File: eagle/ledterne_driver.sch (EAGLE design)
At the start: 1 part, among them IC1 MEGA8-AI

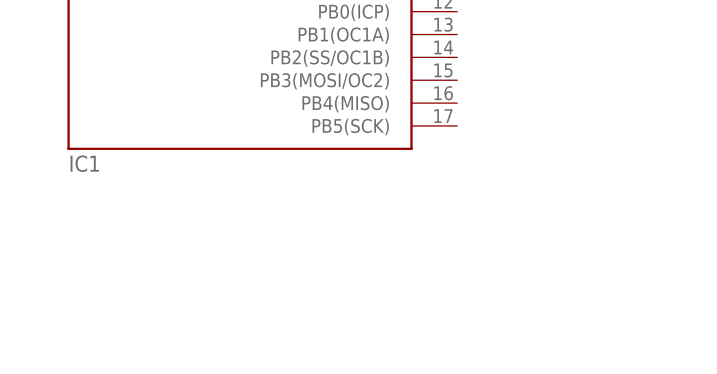
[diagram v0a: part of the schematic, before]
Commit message: Add connectors to the driver board
These connectors will allow the display boards to attach to the
driver board.

Note that this is just a very rough sketch for demonstrating the
basic idea. The exact placement and type of connectors will have
to be fine-tuned later.
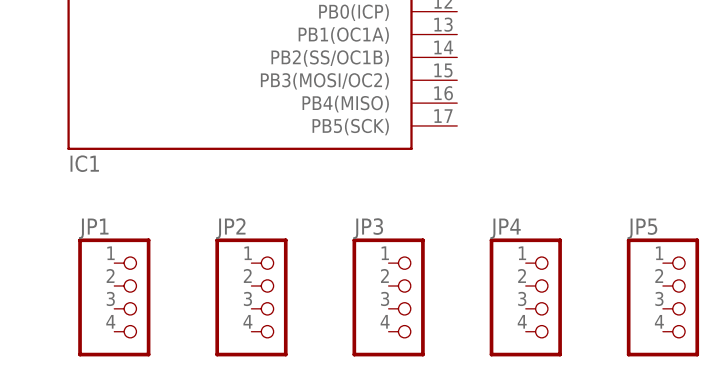
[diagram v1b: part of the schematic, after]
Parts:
- added JP1, JP2, JP3, JP4, JP5: (no value), pinhead:PINHD-1X4/90
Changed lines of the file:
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@@
 <parts>
 <part name="IC1" library="atmel" deviceset="MEGA8" device="-AI"/>
+<part name="JP1" library="pinhead" deviceset="PINHD-1X4" device="/90"/>
+<part name="JP2" library="pinhead" deviceset="PINHD-1X4" device="/90"/>
+<part name="JP3" library="pinhead" deviceset="PINHD-1X4" device="/90"/>
+<part name="JP4" library="pinhead" deviceset="PINHD-1X4" device="/90"/>
+<part name="JP5" library="pinhead" deviceset="PINHD-1X4" device="/90"/>
 </parts>
 <sheets>
@@
 <instances>
 <instance part="IC1" gate="G$1" x="76.2" y="91.44"/>
+<instance part="JP1" gate="A" x="66.04" y="38.1"/>
+<instance part="JP2" gate="A" x="81.28" y="38.1"/>
+<instance part="JP3" gate="A" x="96.52" y="38.1"/>
+<instance part="JP4" gate="A" x="111.76" y="38.1"/>
+<instance part="JP5" gate="A" x="127" y="38.1"/>
 </instances>
 <busses>

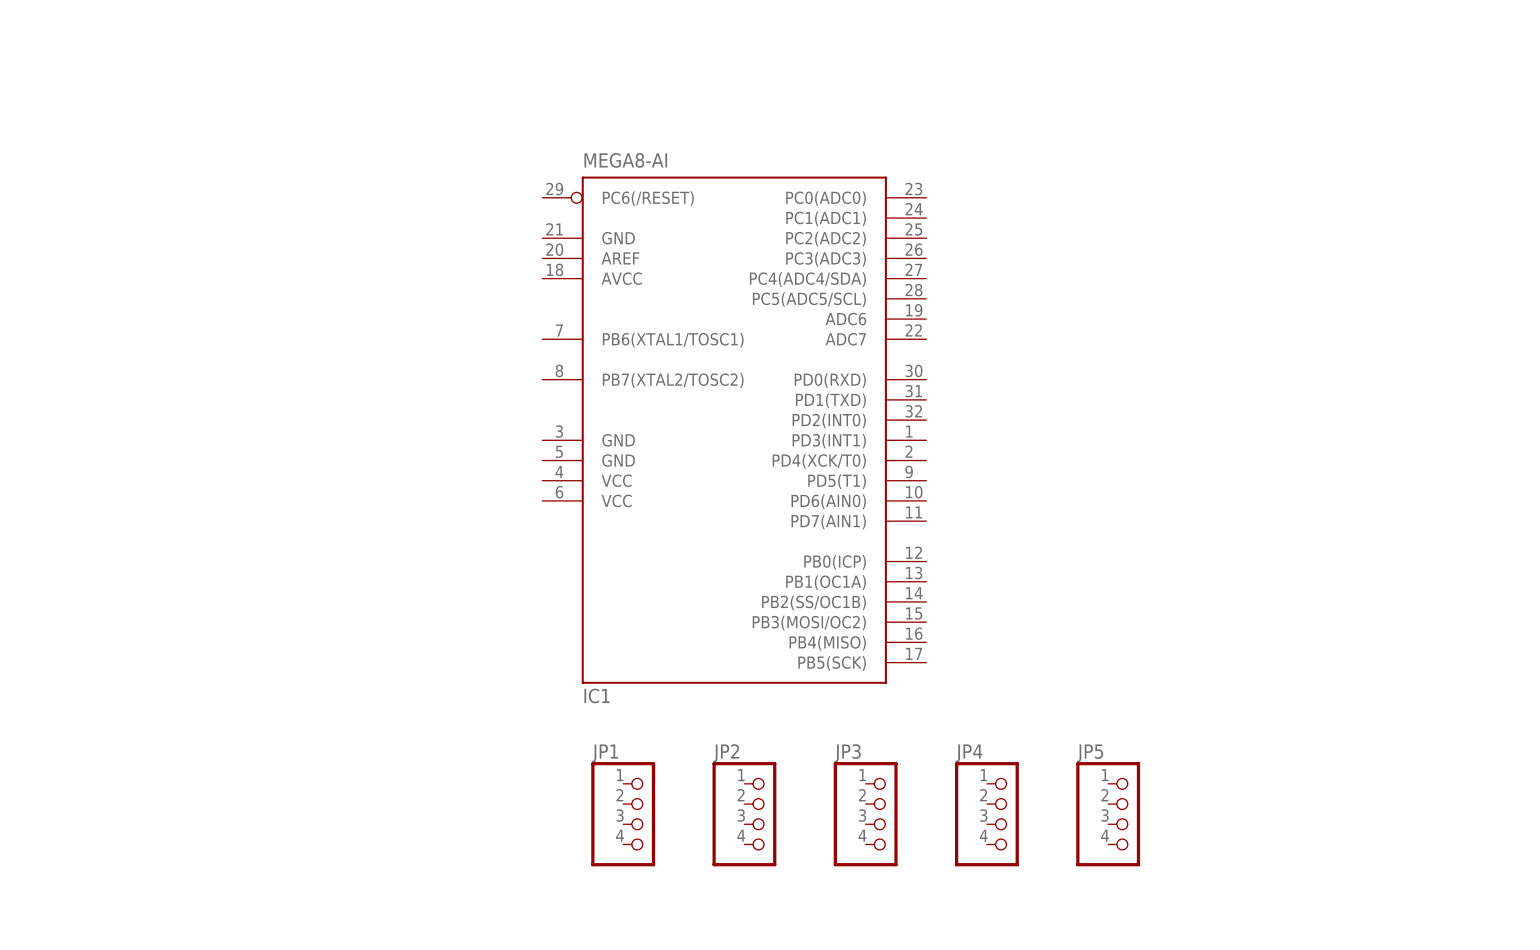
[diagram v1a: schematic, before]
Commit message: Start connecting the components of the driver.
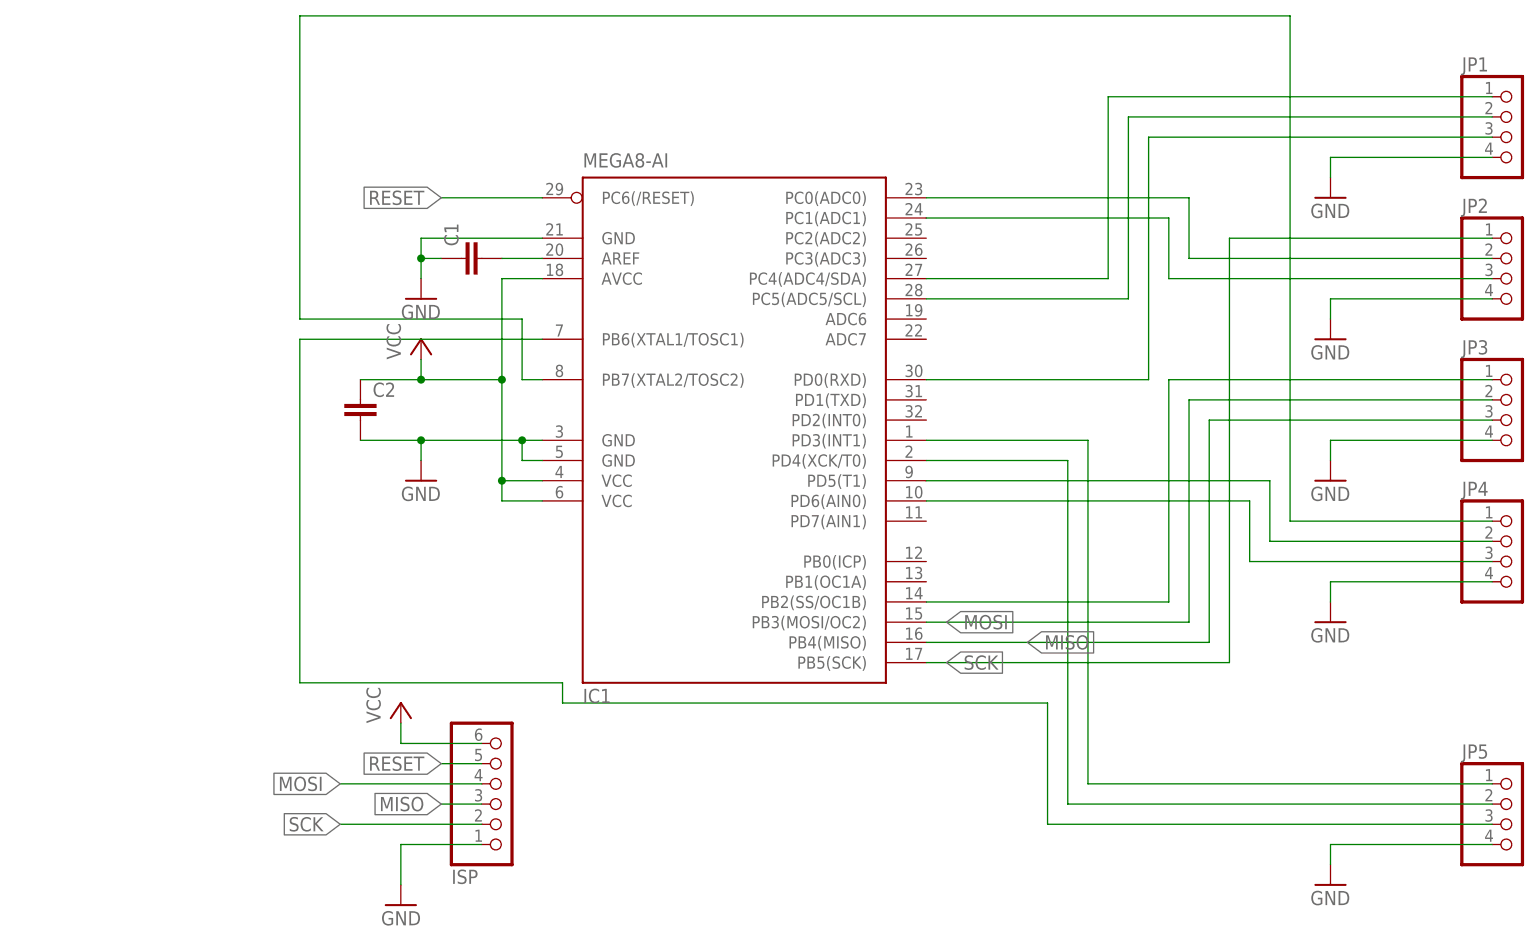
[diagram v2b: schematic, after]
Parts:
- added C1, C2: (no value), rcl:C-EUC0603
- added ISP: (no value), pinhead:PINHD-1X6
- JP1, JP2, JP3, JP4, JP5: device pinhead:PINHD-1X4/90 -> pinhead_round_pads:PINHD-1X4/90
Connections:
- new net GND: C1.1, C2.2, IC1.GND, IC1.GND@1, IC1.GND@2, ISP.1, JP1.4, JP2.4, JP3.4, JP4.4, JP5.4
- new net MISO: IC1.PB4(MISO), ISP.3, JP3.3
- new net MOSI: IC1.PB3(MOSI/OC2), ISP.4, JP3.2
- new net N$1: C1.2, IC1.AREF
- new net N$10: IC1.PD6(AIN0), JP4.3
- new net N$11: IC1.PB6(XTAL1/TOSC1), JP5.3
- new net N$12: IC1.PB7(XTAL2/TOSC2), JP4.1
- new net N$13: IC1.PD3(INT1), JP5.1
- new net N$2: IC1.PD0(RXD), JP1.3
- new net N$3: IC1.PC5(ADC5/SCL), JP1.2
- new net N$4: IC1.PC4(ADC4/SDA), JP1.1
- new net N$5: IC1.PC0(ADC0), JP2.2
- new net N$6: IC1.PD4(XCK/T0), JP5.2
- new net N$7: IC1.PC1(ADC1), JP2.3
- new net N$8: IC1.PB2(SS/OC1B), JP3.1
- new net N$9: IC1.PD5(T1), JP4.2
- new net RESET: IC1.PC6(/RESET), ISP.5
- new net SCK: IC1.PB5(SCK), ISP.2, JP2.1
- new net VCC: C2.1, IC1.AVCC, IC1.VCC@1, IC1.VCC@2, ISP.6
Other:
- moved on the sheet: JP1, JP2, JP3, JP4, JP5

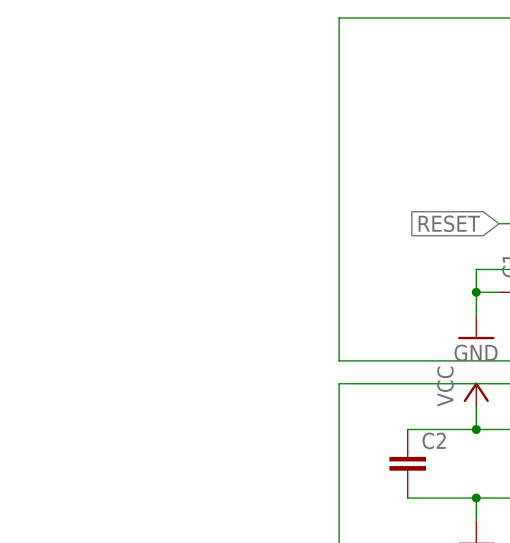
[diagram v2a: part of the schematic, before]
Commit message: Add connector for supply voltage
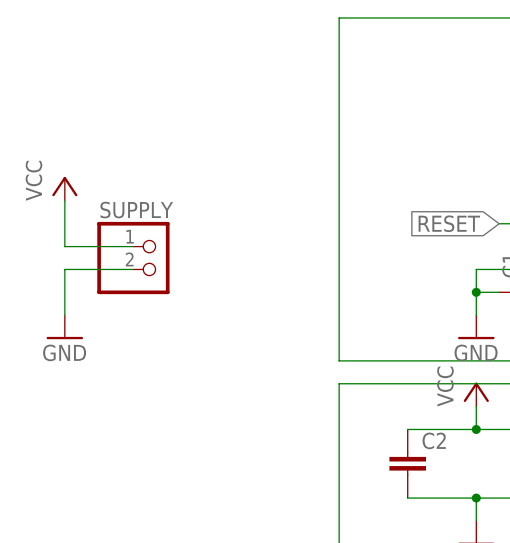
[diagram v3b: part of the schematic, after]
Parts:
- added SUPPLY: (no value), pinhead:PINHD-1X2
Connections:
- net GND: now also SUPPLY.2
- net VCC: now also SUPPLY.1
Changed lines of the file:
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@@
 <?xml version="1.0" encoding="utf-8"?>
 <!DOCTYPE eagle SYSTEM "eagle.dtd">
-<eagle version="7.4.0">
+<eagle version="7.3.0">
 <drawing>
 <settings>
@@
 <part name="JP4" library="pinhead_round_pads" deviceset="PINHD-1X4" device="/90"/>
 <part name="JP5" library="pinhead_round_pads" deviceset="PINHD-1X4" device="/90"/>
+<part name="SUPPLY" library="pinhead" deviceset="PINHD-1X2" device=""/>
+<part name="P+3" library="supply1" deviceset="VCC" device=""/>
+<part name="GND9" library="supply1" deviceset="GND" device=""/>
 </parts>
 <sheets>
@@
 <instance part="JP4" gate="A" x="175.26" y="71.12"/>
 <instance part="JP5" gate="A" x="175.26" y="38.1"/>
+<instance part="SUPPLY" gate="G$1" x="2.54" y="111.76"/>
+<instance part="P+3" gate="VCC" x="-7.62" y="121.92"/>
+<instance part="GND9" gate="1" x="-7.62" y="104.14"/>
 </instances>
 <busses>
@@
 <wire x1="152.4" y1="35.56" x2="152.4" y2="33.02" width="0.1524" layer="91"/>
 <pinref part="JP5" gate="A" pin="4"/>
+</segment>
+<segment>
+<pinref part="SUPPLY" gate="G$1" pin="2"/>
+<wire x1="0" y1="111.76" x2="-7.62" y2="111.76" width="0.1524" layer="91"/>
+<pinref part="GND9" gate="1" pin="GND"/>
+<wire x1="-7.62" y1="111.76" x2="-7.62" y2="106.68" width="0.1524" layer="91"/>
 </segment>
 </net>
@@
 <junction x="38.1" y="93.98"/>
 </segment>
+<segment>
+<pinref part="P+3" gate="VCC" pin="VCC"/>
+<wire x1="-7.62" y1="119.38" x2="-7.62" y2="114.3" width="0.1524" layer="91"/>
+<pinref part="SUPPLY" gate="G$1" pin="1"/>
+<wire x1="-7.62" y1="114.3" x2="0" y2="114.3" width="0.1524" layer="91"/>
+</segment>
 </net>
